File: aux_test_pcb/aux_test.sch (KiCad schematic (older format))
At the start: 12 parts, among them J1 AUX_TEST, J2 SOL, J3 PUMP, J4 SERVO

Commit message: aux_test minor mods
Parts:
- D1: value LEL_SOL -> SOL
- D2: value LED_Vin -> Vin
- D3: value LED_PUMP -> PUMP
- D4: value LED_SVCC -> SVCC
- R1, R2: value 150E -> 390E
- R3, R4: value 150E -> 330E
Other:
- note added: "Vin = 9 V\nSVCC = 6 V"
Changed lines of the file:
@@
 P 4900 4750
 F 0 "D1" V 4975 4675 40  0000 L CNB
-F 1 "LEL_SOL" H 4550 4725 40  0000 L CNB
+F 1 "SOL" H 4550 4725 40  0000 L CNB
 F 2 "aux_test_Libs:LED-5MM" V 4900 4750 50  0001 C CNN
 F 3 "" V 4900 4750 50  0000 C CNN
@@
 P 5200 4750
 F 0 "D2" V 5275 4675 40  0000 L CNB
-F 1 "LED_Vin" H 4850 4725 40  0000 L CNB
+F 1 "Vin" H 4850 4725 40  0000 L CNB
 F 2 "aux_test_Libs:LED-5MM" V 5200 4750 50  0001 C CNN
 F 3 "" V 5200 4750 50  0000 C CNN
@@
 P 5500 4750
 F 0 "D3" V 5575 4675 40  0000 L CNB
-F 1 "LED_PUMP" H 5150 4725 40  0000 L CNB
+F 1 "PUMP" H 5150 4725 40  0000 L CNB
 F 2 "aux_test_Libs:LED-5MM" V 5500 4750 50  0001 C CNN
 F 3 "" V 5500 4750 50  0000 C CNN
@@
 P 5800 4750
 F 0 "D4" V 5875 4675 40  0000 L CNB
-F 1 "LED_SVCC" H 5450 4725 40  0000 L CNB
+F 1 "SVCC" H 5450 4725 40  0000 L CNB
 F 2 "aux_test_Libs:LED-5MM" V 5800 4750 50  0001 C CNN
 F 3 "" V 5800 4750 50  0000 C CNN
@@
 P 4900 5300
 F 0 "R1" H 4950 5375 40  0000 L CNB
-F 1 "150E" V 4900 5300 40  0000 C CNB
+F 1 "390E" V 4900 5300 40  0000 C CNB
 F 2 "aux_test_Libs:Resistor_Horizontal_RM10mm" V 4830 5300 50  0001 C CNN
 F 3 "" H 4900 5300 50  0001 C CNN
@@
 P 5200 5300
 F 0 "R2" H 5250 5375 40  0000 L CNB
-F 1 "150E" V 5200 5300 40  0000 C CNB
+F 1 "390E" V 5200 5300 40  0000 C CNB
 F 2 "aux_test_Libs:Resistor_Horizontal_RM10mm" V 5130 5300 50  0001 C CNN
 F 3 "" H 5200 5300 50  0001 C CNN
@@
 P 5500 5300
 F 0 "R3" H 5550 5375 40  0000 L CNB
-F 1 "150E" V 5500 5300 40  0000 C CNB
+F 1 "330E" V 5500 5300 40  0000 C CNB
 F 2 "aux_test_Libs:Resistor_Horizontal_RM10mm" V 5430 5300 50  0001 C CNN
 F 3 "" H 5500 5300 50  0001 C CNN
@@
 P 5800 5300
 F 0 "R4" H 5850 5375 40  0000 L CNB
-F 1 "150E" V 5800 5300 40  0000 C CNB
+F 1 "330E" V 5800 5300 40  0000 C CNB
 F 2 "aux_test_Libs:Resistor_Horizontal_RM10mm" V 5730 5300 50  0001 C CNN
 F 3 "" H 5800 5300 50  0001 C CNN
@@
 Text Notes 7275 2400 0    100  ~ 20
 OUTPUT
+Text Notes 1700 3150 0    60   ~ 12
+Vin = 9 V\nSVCC = 6 V
 $EndSCHEMATC

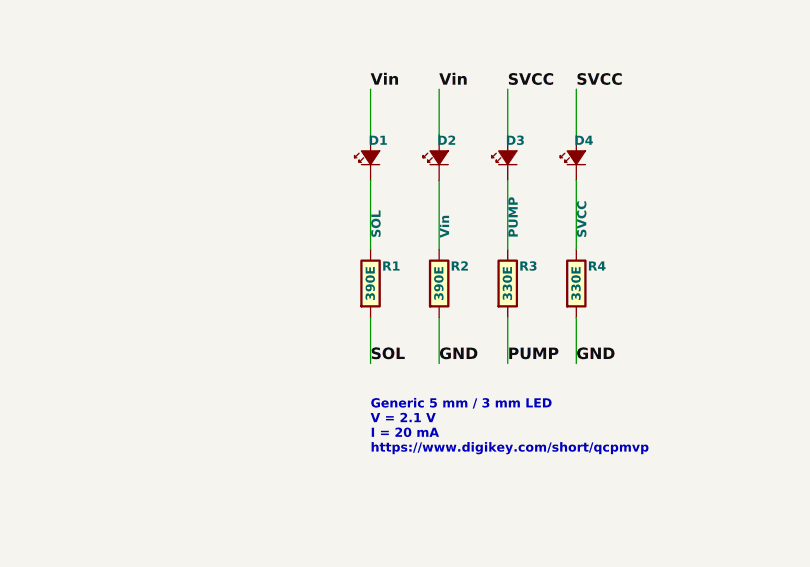
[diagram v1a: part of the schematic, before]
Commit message: updated aux_test PCB
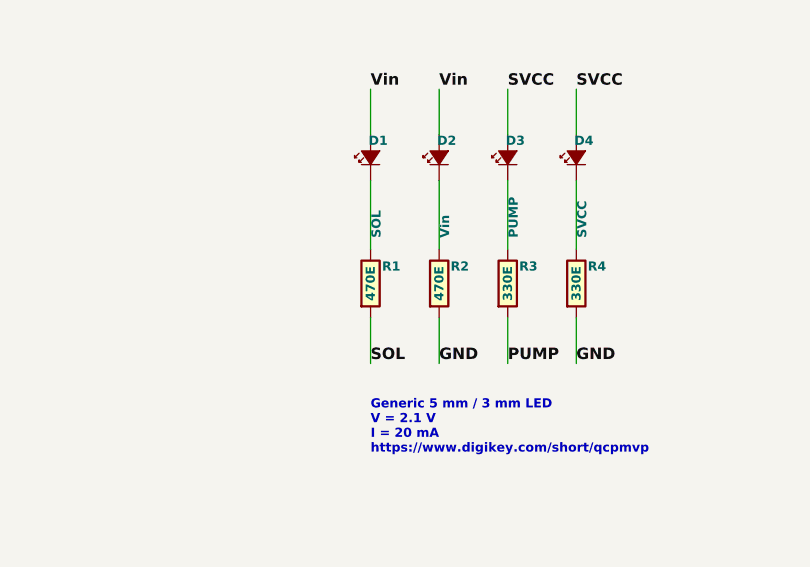
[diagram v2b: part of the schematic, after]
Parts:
- R1, R2: value 390E -> 470E
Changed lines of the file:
@@
 P 4900 5300
 F 0 "R1" H 4950 5375 40  0000 L CNB
-F 1 "390E" V 4900 5300 40  0000 C CNB
+F 1 "470E" V 4900 5300 40  0000 C CNB
 F 2 "aux_test_Libs:Resistor_Horizontal_RM10mm" V 4830 5300 50  0001 C CNN
 F 3 "" H 4900 5300 50  0001 C CNN
@@
 P 5200 5300
 F 0 "R2" H 5250 5375 40  0000 L CNB
-F 1 "390E" V 5200 5300 40  0000 C CNB
+F 1 "470E" V 5200 5300 40  0000 C CNB
 F 2 "aux_test_Libs:Resistor_Horizontal_RM10mm" V 5130 5300 50  0001 C CNN
 F 3 "" H 5200 5300 50  0001 C CNN
